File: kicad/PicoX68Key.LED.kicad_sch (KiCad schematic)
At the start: 22 parts, among them J1 LED_BOARD, U1 74HCT595, U2 74HCT595

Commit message: Create LED board and tweak designs
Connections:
- no-connect marks 2 -> 4
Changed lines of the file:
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@@
 		(at 62.23 125.73)
+	)
+	(no_connect
+		(at 118.11 130.81)
+	)
+	(no_connect
+		(at 118.11 80.01)
 	)
 	(bus_entry

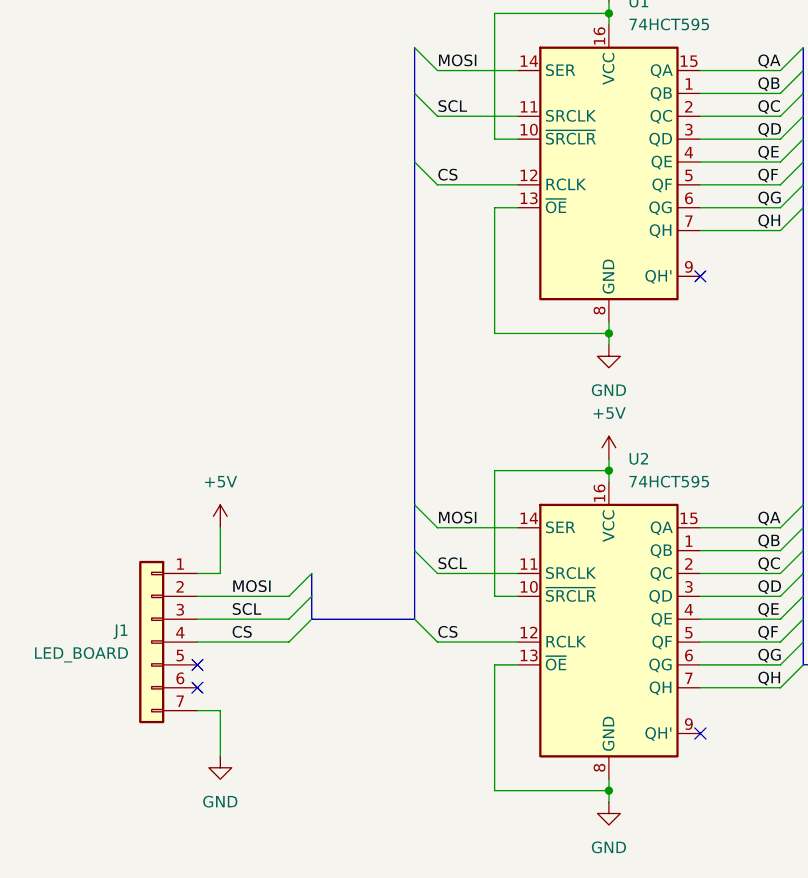
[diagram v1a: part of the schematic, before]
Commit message: Add PWM functionality to set LED brightness
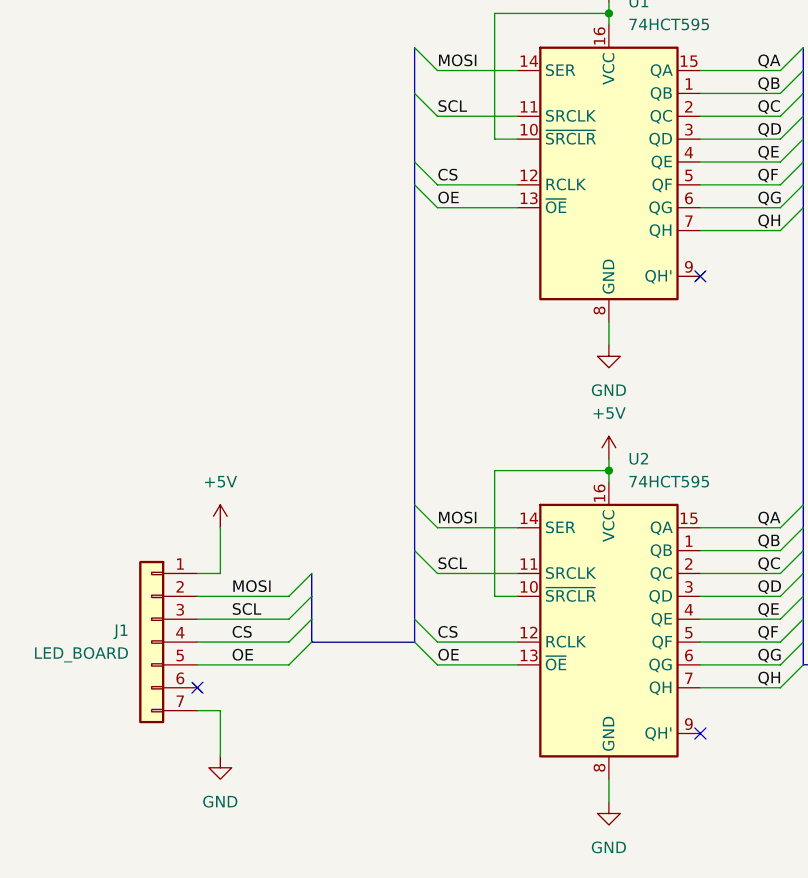
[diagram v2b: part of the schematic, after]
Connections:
- net GND: no longer U1.13 (~{OE}), U2.13 (~{OE})
- net OE: now reaches J1.5 (Pin_5)
- net OE: now also U1.13 (~{OE}), U2.13 (~{OE})
- no-connect marks 4 -> 3
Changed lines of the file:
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@@
-	)
-	(junction
-		(at 107.95 137.16)
-		(diameter 0)
-		(color 0 0 0 0)
 	)
 	(junction
@@
 	)
 	(junction
-		(at 107.95 86.36)
-		(diameter 0)
-		(color 0 0 0 0)
-	)
-	(junction
 		(at 195.58 62.23)
 		(diameter 0)
@@
 	)
 	(no_connect
-		(at 62.23 123.19)
-	)
-	(no_connect
 		(at 62.23 125.73)
 	)
@@
 	)
 	(bus_entry
+		(at 74.93 120.65)
+		(size -2.54 2.54)
+		(stroke
+			(width 0)
+			(type default)
+		)
+	)
+	(bus_entry
 		(at 86.36 59.69)
 		(size 2.54 2.54)
@@
 	)
 	(bus_entry
+		(at 86.36 69.85)
+		(size 2.54 2.54)
+		(stroke
+			(width 0)
+			(type default)
+		)
+	)
+	(bus_entry
+		(at 86.36 120.65)
+		(size 2.54 2.54)
+		(stroke
+			(width 0)
+			(type default)
+		)
+	)
+	(bus_entry
 		(at 86.36 110.49)
 		(size 2.54 2.54)
@@
 	(wire
 		(pts
-			(xy 107.95 85.09) (xy 107.95 86.36)
+			(xy 107.95 85.09) (xy 107.95 87.63)
 		)
 		(stroke
@@
 		)
 	)
-	(wire
-		(pts
-			(xy 107.95 86.36) (xy 107.95 87.63)
-		)
-		(stroke
-			(width 0)
-			(type default)
-		)
-	)
 	(bus
 		(pts
@@
 	(wire
 		(pts
-			(xy 95.25 123.19) (xy 95.25 137.16)
+			(xy 88.9 72.39) (xy 97.79 72.39)
 		)
 		(stroke
@@
 	(wire
 		(pts
-			(xy 107.95 135.89) (xy 107.95 137.16)
-		)
-		(stroke
-			(width 0)
-			(type default)
-		)
-	)
-	(bus
-		(pts
-			(xy 86.36 67.31) (xy 86.36 105.41)
+			(xy 107.95 135.89) (xy 107.95 138.43)
+		)
+		(stroke
+			(width 0)
+			(type default)
+		)
+	)
+	(bus
+		(pts
+			(xy 86.36 67.31) (xy 86.36 69.85)
 		)
 		(stroke
@@
 		)
 	)
+	(bus
+		(pts
+			(xy 86.36 69.85) (xy 86.36 105.41)
+		)
+		(stroke
+			(width 0)
+			(type default)
+		)
+	)
 	(wire
 		(pts
@@
 		)
 	)
-	(wire
-		(pts
-			(xy 95.25 72.39) (xy 97.79 72.39)
-		)
-		(stroke
-			(width 0)
-			(type default)
-		)
-	)
 	(bus
 		(pts
@@
 	(bus
 		(pts
-			(xy 86.36 118.11) (xy 74.93 118.11)
+			(xy 86.36 120.65) (xy 74.93 120.65)
 		)
 		(stroke
@@
 	(wire
 		(pts
+			(xy 62.23 123.19) (xy 72.39 123.19)
+		)
+		(stroke
+			(width 0)
+			(type default)
+		)
+	)
+	(wire
+		(pts
 			(xy 193.04 135.89) (xy 195.58 135.89)
 		)
@@
 	(wire
 		(pts
-			(xy 107.95 86.36) (xy 95.25 86.36)
-		)
-		(stroke
-			(width 0)
-			(type default)
-		)
-	)
-	(wire
-		(pts
 			(xy 195.58 100.33) (xy 195.58 125.73)
 		)
@@
 		)
 	)
+	(bus
+		(pts
+			(xy 74.93 118.11) (xy 74.93 120.65)
+		)
+		(stroke
+			(width 0)
+			(type default)
+		)
+	)
 	(wire
 		(pts
@@
 	(wire
 		(pts
-			(xy 107.95 137.16) (xy 107.95 138.43)
-		)
-		(stroke
-			(width 0)
-			(type default)
-		)
-	)
-	(wire
-		(pts
 			(xy 107.95 101.6) (xy 107.95 102.87)
 		)
@@
 	(wire
 		(pts
+			(xy 88.9 123.19) (xy 97.79 123.19)
+		)
+		(stroke
+			(width 0)
+			(type default)
+		)
+	)
+	(wire
+		(pts
 			(xy 205.74 72.39) (xy 205.74 43.18)
 		)
@@
 	(wire
 		(pts
-			(xy 95.25 137.16) (xy 107.95 137.16)
-		)
-		(stroke
-			(width 0)
-			(type default)
-		)
-	)
-	(wire
-		(pts
-			(xy 95.25 86.36) (xy 95.25 72.39)
-		)
-		(stroke
-			(width 0)
-			(type default)
-		)
-	)
-	(wire
-		(pts
 			(xy 200.66 105.41) (xy 200.66 125.73)
 		)
@@
 		)
 	)
+	(bus
+		(pts
+			(xy 86.36 118.11) (xy 86.36 120.65)
+		)
+		(stroke
+			(width 0)
+			(type default)
+		)
+	)
 	(wire
 		(pts
@@
 		(pts
 			(xy 205.74 72.39) (xy 205.74 110.49)
-		)
-		(stroke
-			(width 0)
-			(type default)
-		)
-	)
-	(wire
-		(pts
-			(xy 97.79 123.19) (xy 95.25 123.19)
 		)
 		(stroke
@@
 		)
 	)
+	(label "OE"
+		(at 66.04 123.19 0)
+		(effects
+			(font
+				(size 1.27 1.27)
+			)
+			(justify left bottom)
+		)
+	)
 	(label "QA"
 		(at 124.46 107.95 0)
@@
 		)
 	)
+	(label "OE"
+		(at 88.9 123.19 0)
+		(effects
+			(font
+				(size 1.27 1.27)
+			)
+			(justify left bottom)
+		)
+	)
 	(label "CS"
 		(at 88.9 120.65 0)
@@
 		(effects
 			(font
+				(size 1.27 1.27)
+			)
+			(justify left bottom)
+		)
+	)
+	(label "OE"
+		(at 88.9 72.39 0)
+		(effects
+			(font
